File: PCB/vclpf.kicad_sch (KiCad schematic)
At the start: 16 parts, among them J7 VCLPF, Q8 2N5457, U2 LM324

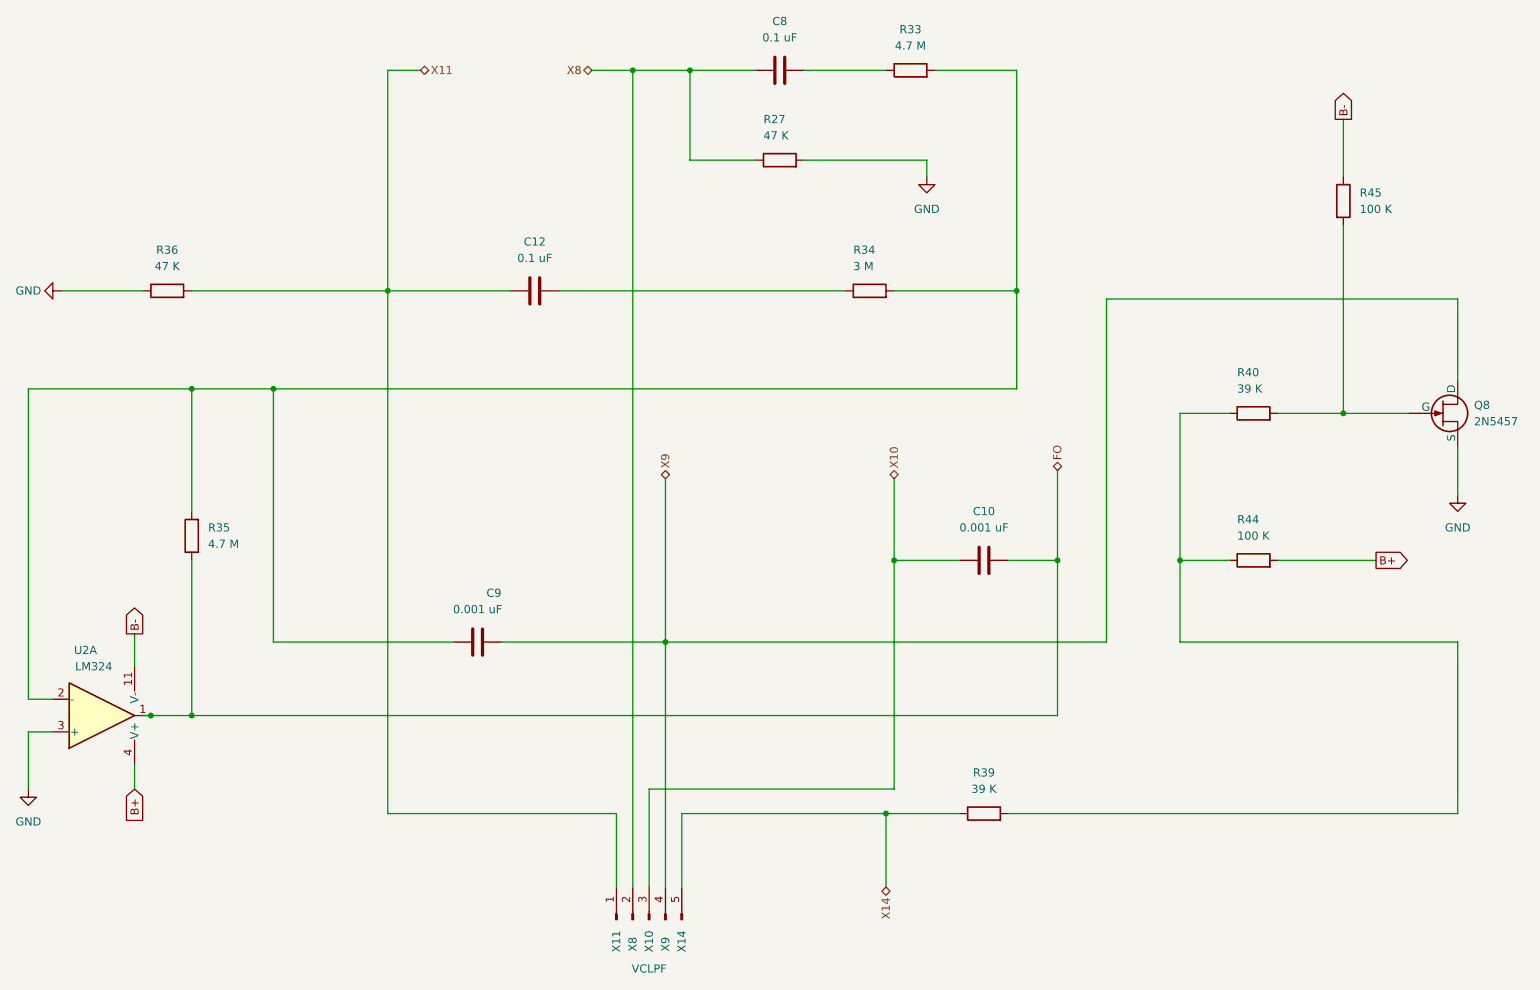
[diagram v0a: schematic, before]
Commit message: Change TO-92 transistors to wide package to avoid shorting during soldering
Added B- hole for speaker
Added more vias to shorten traces
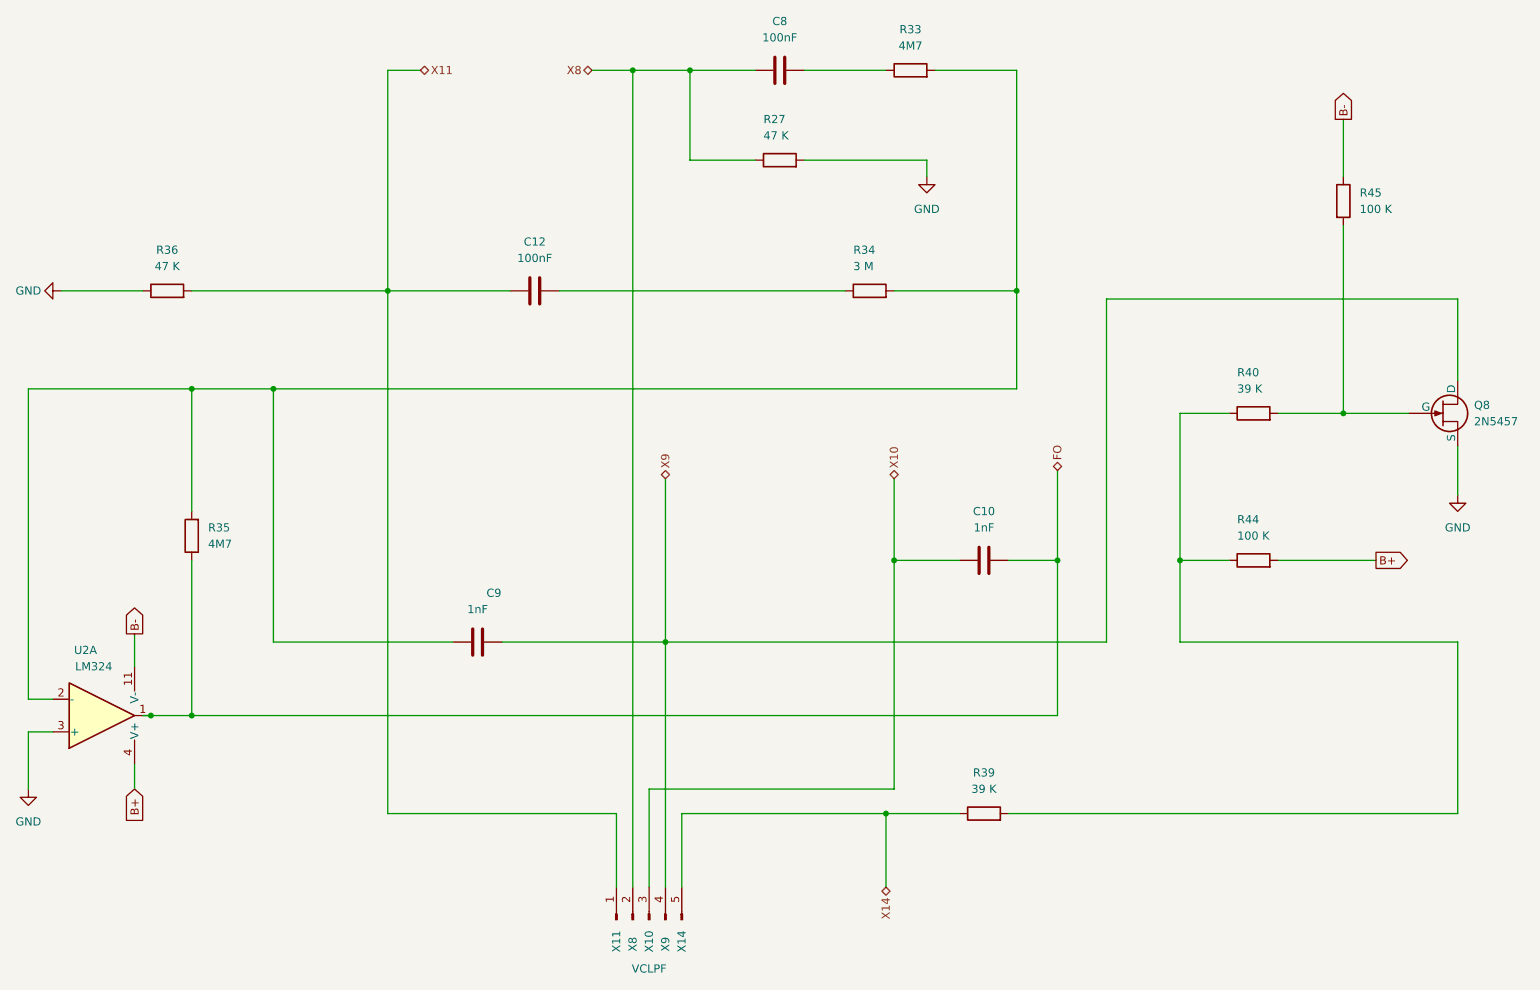
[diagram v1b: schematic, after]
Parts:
- C10, C9: value 0.001 uF -> 1nF
- C12, C8: value 0.1 uF -> 100nF
- R33, R35: value 4.7 M -> 4M7
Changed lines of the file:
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@@
 			)
 		)
-		(property "Value" "0.001 uF"
+		(property "Value" "1nF"
 			(at 180.34 109.22 90)
 			(show_name no)
@@
 		(fields_autoplaced yes)
 		(property "Reference" "R35"
-			(at 59.69 109.22 0)
+			(at 59.69 109.2199 0)
 			(show_name no)
 			(do_not_autoplace no)
@@
 			)
 		)
-		(property "Value" "4.7 M"
-			(at 59.69 111.76 0)
+		(property "Value" "4M7"
+			(at 59.69 111.7599 0)
 			(show_name no)
 			(do_not_autoplace no)
@@
 			)
 		)
-		(property "Value" "0.1 uF"
+		(property "Value" "100nF"
 			(at 148.59 33.02 90)
 			(show_name no)
@@
 			)
 		)
-		(property "Value" "0.001 uF"
+		(property "Value" "1nF"
 			(at 101.6 121.92 90)
 			(show_name no)
@@
 			)
 		)
-		(property "Value" "4.7 M"
+		(property "Value" "4M7"
 			(at 168.91 34.29 90)
 			(show_name no)
@@
 			)
 		)
-		(property "Value" "0.1 uF"
+		(property "Value" "100nF"
 			(at 110.49 67.31 90)
 			(show_name no)

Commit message: Necessary Changes to Schematic and PCB
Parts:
- removed J7: VCLPF, Connector_PinHeader_2.00mm:PinHeader_1x05_P2.00mm_Vertical, symbol Connector:Conn_01x05_Pin
- added C28: 100nF, Capacitor_THT:C_Disc_D5.1mm_W3.2mm_P5.00mm, symbol Device:C
- added J7: LPF, Connector_PinSocket_2.54mm:PinSocket_1x06_P2.54mm_Vertical, symbol Connector:Conn_01x06_Pin
- added VCF1: 3 M, Resistor_THT:R_Axial_DIN0207_L6.3mm_D2.5mm_P10.16mm_Horizontal, symbol Device:R
- Q8: footprint Package_TO_SOT_THT:TO-92_Inline -> Package_TO_SOT_THT:TO-92_Inline_Wide; symbol Simulation_SPICE:NJFET -> Device:Q_NJFET_DSG
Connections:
- net GND: now also Q8.2 (S); no longer Q8.3 (S)
- net X10: now also J7.4 (Pin_4)
- net X11: now also J7.2 (Pin_2)
- net X14: now also J7.6 (Pin_6)
- net X8: now also J7.3 (Pin_3)
- net X9: now also J7.5 (Pin_5)
- net at C9.2, R33.2, R34.2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: now also VCF1.1
- net at R40.2, R45.2: now also Q8.3 (G); no longer Q8.2 (G)
- new net: C28.1, VCF1.2
- new net: C28.2, J7.1 (Pin_1)

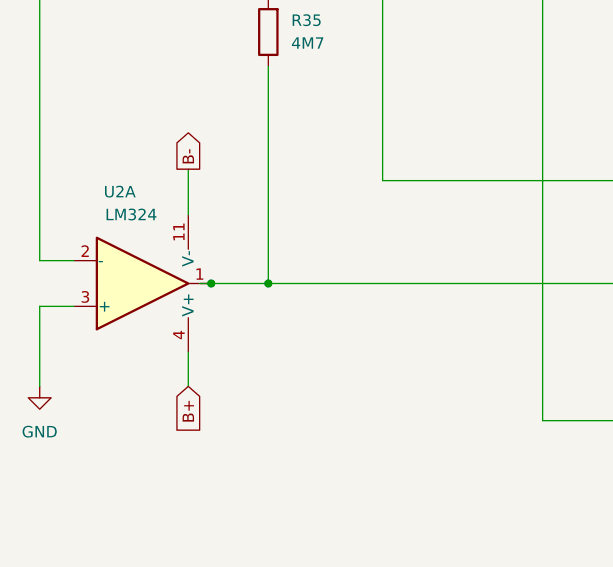
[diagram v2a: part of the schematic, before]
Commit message: Final Update
Move power pins closer to filter caps
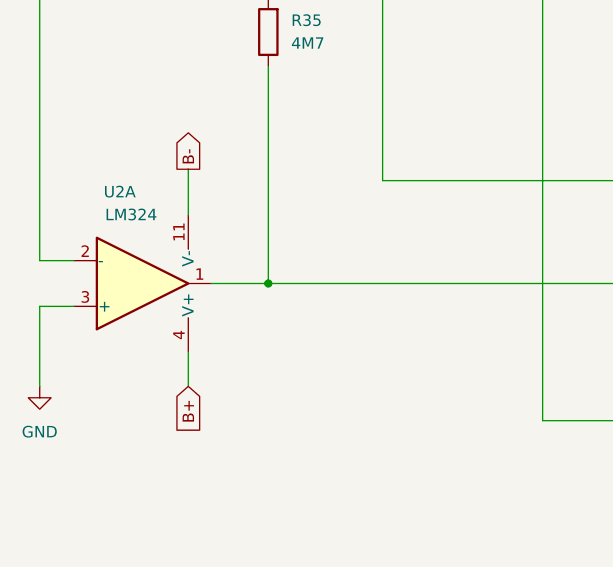
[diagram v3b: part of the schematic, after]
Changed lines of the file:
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@@
-	)
-	(junction
-		(at 50.8 138.43)
-		(diameter 0)
-		(color 0 0 0 0)
 	)
 	(junction
@@
 	)
 	(junction
+		(at 57.15 138.43)
+		(diameter 0)
+		(color 0 0 0 0)
+	)
+	(junction
 		(at 210.82 114.3)
 		(diameter 0)
@@
 	)
 	(junction
-		(at 57.15 138.43)
-		(diameter 0)
-		(color 0 0 0 0)
-	)
-	(junction
 		(at 130.81 127)
 		(diameter 0)
@@
 	(wire
 		(pts
+			(xy 50.8 138.43) (xy 57.15 138.43)
+		)
+		(stroke
+			(width 0)
+			(type default)
+		)
+	)
+	(wire
+		(pts
 			(xy 120.65 144.78) (xy 120.65 165.1)
 		)
@@
 	(wire
 		(pts
+			(xy 196.85 118.11) (xy 196.85 144.78)
+		)
+		(stroke
+			(width 0)
+			(type dash)
+		)
+	)
+	(wire
+		(pts
 			(xy 87.63 38.1) (xy 87.63 72.39)
 		)
@@
 	(wire
 		(pts
-			(xy 49.53 138.43) (xy 50.8 138.43)
-		)
-		(stroke
-			(width 0)
-			(type default)
-		)
-	)
-	(wire
-		(pts
 			(xy 166.37 101.6) (xy 166.37 114.3)
 		)
@@
 	(wire
 		(pts
-			(xy 196.85 118.11) (xy 196.85 144.78)
-		)
-		(stroke
-			(width 0)
-			(type dash)
-		)
-	)
-	(wire
-		(pts
 			(xy 191.77 138.43) (xy 191.77 114.3)
 		)
@@
 		)
 		(stroke
-			(width 0)
-			(type default)
-		)
-	)
-	(wire
-		(pts
-			(xy 50.8 138.43) (xy 57.15 138.43)
-		)
-		(stroke
